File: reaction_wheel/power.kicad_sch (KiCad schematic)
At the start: 3 parts, among them U7 TPS62902RPJR, U9 TPS61379QWRTERQ1

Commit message: things were not working on desktop
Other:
- moved on the sheet: C1, U7
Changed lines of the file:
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@@
 	(paper "A4")
 	(no_connect
-		(at 248.92 39.37)
+		(at 91.44 30.48)
 	)
 	(wire
 		(pts
-			(xy 248.92 41.91) (xy 264.16 41.91)
+			(xy 91.44 33.02) (xy 106.68 33.02)
 		)
 		(stroke
@@
 	(wire
 		(pts
-			(xy 194.31 48.26) (xy 194.31 46.99)
+			(xy 36.83 39.37) (xy 36.83 38.1)
 		)
 		(stroke
@@
 	(wire
 		(pts
-			(xy 264.16 52.07) (xy 264.16 49.53)
+			(xy 106.68 43.18) (xy 106.68 40.64)
 		)
 		(stroke
@@
 	(wire
 		(pts
-			(xy 194.31 46.99) (xy 198.12 46.99)
+			(xy 36.83 38.1) (xy 40.64 38.1)
 		)
 		(stroke
@@
 	(symbol
 		(lib_id "Device:C")
-		(at 264.16 45.72 0)
+		(at 106.68 36.83 0)
 		(unit 1)
 		(body_style 1)
@@
 		(fields_autoplaced yes)
 		(property "Reference" "C1"
-			(at 267.97 44.4499 0)
+			(at 110.49 35.5599 0)
 			(show_name no)
 			(do_not_autoplace no)
@@
 		)
 		(property "Value" "2.2nF"
-			(at 267.97 46.9899 0)
+			(at 110.49 38.0999 0)
 			(show_name no)
 			(do_not_autoplace no)
@@
 		)
 		(property "Footprint" ""
-			(at 265.1252 49.53 0)
+			(at 107.6452 40.64 0)
 			(hide yes)
 			(show_name no)
@@
 		)
 		(property "Datasheet" ""
-			(at 264.16 45.72 0)
+			(at 106.68 36.83 0)
 			(hide yes)
 			(show_name no)
@@
 		)
 		(property "Description" "Unpolarized capacitor"
-			(at 264.16 45.72 0)
+			(at 106.68 36.83 0)
 			(hide yes)
 			(show_name no)
@@
 	(symbol
 		(lib_id "tps62902:TPS62902RPJR")
-		(at 198.12 39.37 0)
+		(at 40.64 30.48 0)
 		(unit 1)
 		(body_style 1)
@@
 		(fields_autoplaced yes)
 		(property "Reference" "U7"
-			(at 223.52 29.21 0)
+			(at 66.04 20.32 0)
 			(show_name no)
 			(do_not_autoplace no)
@@
 		)
 		(property "Value" "TPS62902RPJR"
-			(at 223.52 31.75 0)
+			(at 66.04 22.86 0)
 			(show_name no)
 			(do_not_autoplace no)
@@
 		)
 		(property "Footprint" "QFN_902RPJR_TEX"
-			(at 198.12 39.37 0)
+			(at 40.64 30.48 0)
 			(hide yes)
 			(show_name no)
@@
 		)
 		(property "Datasheet" "https://www.ti.com/lit/gpn/tps62902"
-			(at 198.12 39.37 0)
+			(at 40.64 30.48 0)
 			(hide yes)
 			(show_name no)
@@
 		)
 		(property "Description" ""
-			(at 198.12 39.37 0)
+			(at 40.64 30.48 0)
 			(hide yes)
 			(show_name no)
@@
 	(symbol
 		(lib_id "power:GND")
-		(at 194.31 48.26 0)
+		(at 36.83 39.37 0)
 		(unit 1)
 		(body_style 1)
@@
 		(fields_autoplaced yes)
 		(property "Reference" "#PWR022"
-			(at 194.31 54.61 0)
+			(at 36.83 45.72 0)
 			(hide yes)
 			(show_name no)
@@
 		)
 		(property "Value" "GND"
-			(at 194.31 53.34 0)
+			(at 36.83 44.45 0)
 			(show_name no)
 			(do_not_autoplace no)
@@
 		)
 		(property "Footprint" ""
-			(at 194.31 48.26 0)
+			(at 36.83 39.37 0)
 			(hide yes)
 			(show_name no)
@@
 		)
 		(property "Datasheet" ""
-			(at 194.31 48.26 0)
+			(at 36.83 39.37 0)
 			(hide yes)
 			(show_name no)
@@
 		)
 		(property "Description" "Power symbol creates a global label with name \"GND\" , ground"
-			(at 194.31 48.26 0)
+			(at 36.83 39.37 0)
 			(hide yes)
 			(show_name no)
@@
 	(symbol
 		(lib_id "power:GND")
-		(at 264.16 52.07 0)
+		(at 106.68 43.18 0)
 		(unit 1)
 		(body_style 1)
@@
 		(fields_autoplaced yes)
 		(property "Reference" "#PWR023"
-			(at 264.16 58.42 0)
+			(at 106.68 49.53 0)
 			(hide yes)
 			(show_name no)
@@
 		)
 		(property "Value" "GND"
-			(at 264.16 57.15 0)
+			(at 106.68 48.26 0)
 			(show_name no)
 			(do_not_autoplace no)
@@
 		)
 		(property "Footprint" ""
-			(at 264.16 52.07 0)
+			(at 106.68 43.18 0)
 			(hide yes)
 			(show_name no)
@@
 		)
 		(property "Datasheet" ""
-			(at 264.16 52.07 0)
+			(at 106.68 43.18 0)
 			(hide yes)
 			(show_name no)
@@
 		)
 		(property "Description" "Power symbol creates a global label with name \"GND\" , ground"
-			(at 264.16 52.07 0)
-			(hide yes)
-			(show_name no)
+			(at 106.68 43.18 0)
+			(hide yes)
+			(show_name no)

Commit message: Add files via upload
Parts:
- removed C1: 2.2nF, symbol Device:C
- removed U7: TPS62902RPJR, QFN_902RPJR_TEX, symbol tps62902:TPS62902RPJR
- removed U9: TPS61379QWRTERQ1, RTE0016K-IPC_A, symbol TPS62902RPJR_boost_converter:TPS61379QWRTERQ1
- added C36: 10uF, symbol Device:C
- added C37: 10nF, symbol Device:C
- added C38, C39, C44: 22uF, symbol Device:C
- added C40: 4.7nF, symbol Device:C
- added C41: 0.1uF, symbol Device:C
- added C42: 2.2uF, symbol Device:C
- added C43: 1uF, symbol Device:C
- added J12: 5013310207, CONN_5013310000-SD_02_MOL, symbol molex_pico_clasp:5013310207
- added L5, L6: 1uH, symbol Device:L
- added R27: 26.1k, symbol Device:R
- added R35, R37: 100k, symbol Device:R
- added R36: 10k, symbol Device:R
- added R38: 18k, symbol Device:R
- added R39: 280k, symbol Device:R
- added R40: 20k, symbol Device:R
- added U12: TPS62902RPJR, QFN_902RPJR_TEX, symbol tps62902:TPS62902RPJR
- added U13: TPS61379QWRTERQ1, RTE0016K-IPC_A, symbol TPS62902RPJR_boost_converter:TPS61379QWRTERQ1
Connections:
- net GND: now also C36.2, C37.2, C38.2, C39.2, C40.2, C42.2, C43.2, C44.2, J12.2, R27.2, R38.2, R40.2, U12.4 (GND), U13.17 (Thermal_Pad), U13.5 (MODE_SYNC), U13.7 (GND), U13.8 (GND)
- new net: C40.1, R36.2
- new net +12V: C43.1, C44.1, R39.1, U13.10 (OUT), U13.9 (VO)
- new net +3V3: C38.1, L5.2, U12.3 (VOS)
- new net BST_Boost: C41.2, U13.2 (BST)
- new net COMP_Boost: R36.1, U13.14 (COMP)
- new net EN_Boost: R35.2, U13.15 (EN)
- new net FB_Boost: R39.2, R40.1, U13.13 (FB)
- new net FREQ_Boost: R38.1, U13.16 (FREQ)
- new net MODE_SCONF_Buck: R27.1, U12.7 (MODE/S-CONF)
- new net PG_Boost: R37.1, U13.11 (PG)
- new net SS_TR_Buck: C37.1, U12.8 (SS/TR)
- new net SW_Boost: C41.1, L6.2, U13.3 (SW), U13.4 (SW)
- new net SW_Buck: L5.1, U12.2 (SW)
- new net VBATT: C36.1, C39.1, J12.1, L6.1, R35.1, U12.5 (EN), U12.6 (VIN), U13.1 (VIN)
- new net VCC_Boost: C42.1, R37.2, U13.6 (VCC)
- no-connect marks 1 -> 3
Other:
- note added: "Battery Connector to ADCS Board"
- note added: "Boost Converter: Battery to +12V"
- note added: "Buck Converter: Battery to +3V3"
- note added: "For C27 (10uF cap), select a ceramic capacitor rated for at least 16V or 25V (X7R or X5R dielectric). Ceramic capacitors lose effective capacitance under DC bias voltage; a 10V-rated capacitor will drop below the minimum required capacitance when operating at 8V input."
- note added: "SS/TR: do i need soft time start thing? for 1ms = 10nF else can leave open?"
- note added: "molex pico clasp connector"

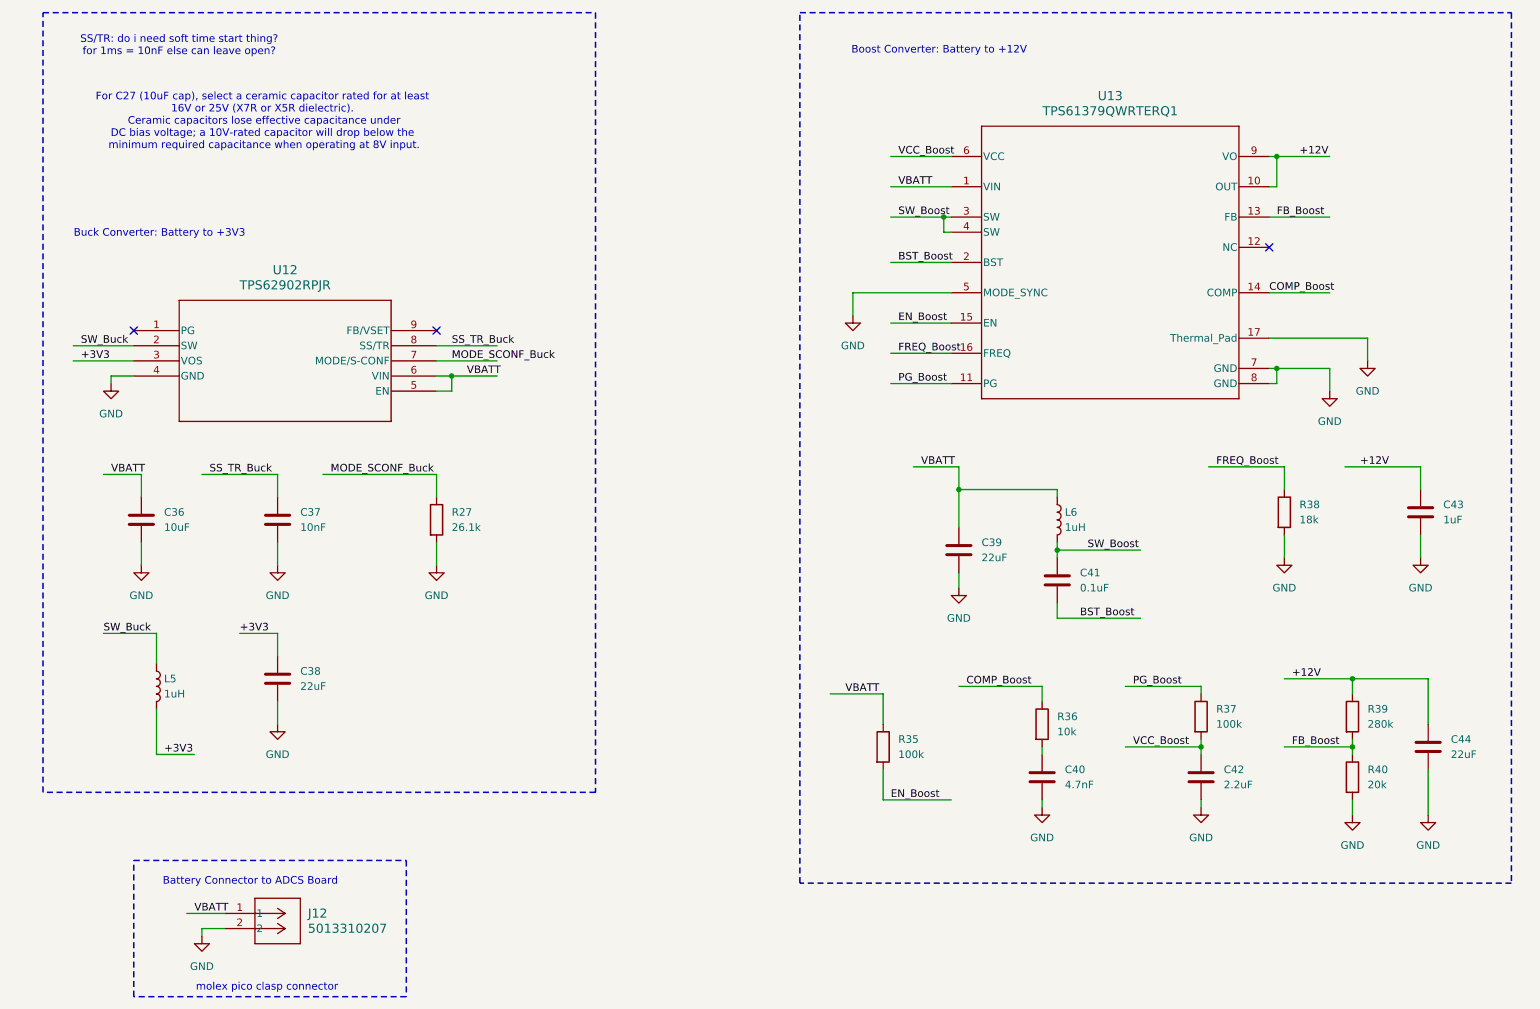
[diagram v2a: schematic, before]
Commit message: clean up sch, notes, added parts minus stlink
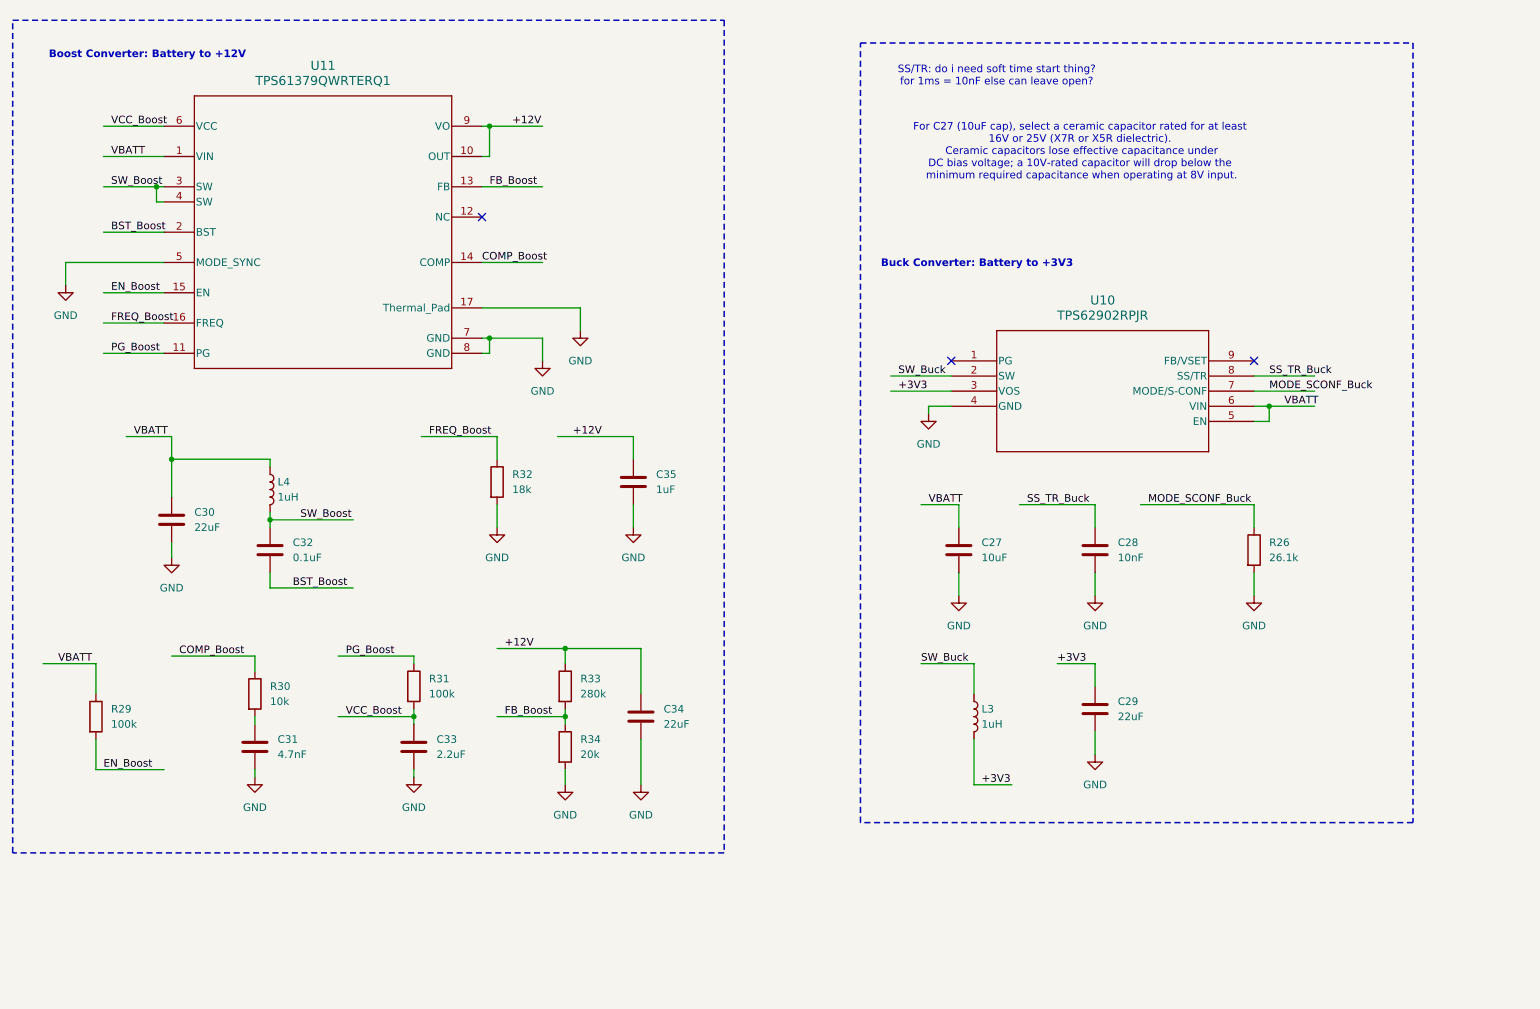
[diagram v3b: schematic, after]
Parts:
- removed C36: 10uF, symbol Device:C
- removed C37: 10nF, symbol Device:C
- removed C38, C39, C44: 22uF, symbol Device:C
- removed C40: 4.7nF, symbol Device:C
- removed C41: 0.1uF, symbol Device:C
- removed C42: 2.2uF, symbol Device:C
- removed C43: 1uF, symbol Device:C
- removed J12: 5013310207, CONN_5013310000-SD_02_MOL, symbol molex_pico_clasp:5013310207
- removed L5, L6: 1uH, symbol Device:L
- removed R27: 26.1k, symbol Device:R
- removed R35, R37: 100k, symbol Device:R
- removed R36: 10k, symbol Device:R
- removed R38: 18k, symbol Device:R
- removed R39: 280k, symbol Device:R
- removed R40: 20k, symbol Device:R
- removed U12: TPS62902RPJR, QFN_902RPJR_TEX, symbol tps62902:TPS62902RPJR
- removed U13: TPS61379QWRTERQ1, RTE0016K-IPC_A, symbol TPS62902RPJR_boost_converter:TPS61379QWRTERQ1
- added C27: 10uF, symbol Device:C
- added C28: 10nF, symbol Device:C
- added C29, C30, C34: 22uF, symbol Device:C
- added C31: 4.7nF, symbol Device:C
- added C32: 0.1uF, symbol Device:C
- added C33: 2.2uF, symbol Device:C
- added C35: 1uF, symbol Device:C
- added L3, L4: 1uH, symbol Device:L
- added R26: 26.1k, symbol Device:R
- added R29, R31: 100k, symbol Device:R
- added R30: 10k, symbol Device:R
- added R32: 18k, symbol Device:R
- added R33: 280k, symbol Device:R
- added R34: 20k, symbol Device:R
- added U10: TPS62902RPJR, QFN_902RPJR_TEX, symbol tps62902:TPS62902RPJR
- added U11: TPS61379QWRTERQ1, RTE0016K-IPC_A, symbol TPS62902RPJR_boost_converter:TPS61379QWRTERQ1
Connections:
- net +12V: now also C34.1, C35.1, R33.1, U11.10 (OUT), U11.9 (VO)
- net +3V3: now also C29.1, L3.2, U10.3 (VOS)
- net BST_Boost: now also C32.2, U11.2 (BST)
- net COMP_Boost: now also R30.1, U11.14 (COMP)
- net EN_Boost: now also R29.2, U11.15 (EN)
- net FB_Boost: now also R33.2, R34.1, U11.13 (FB)
- net FREQ_Boost: now also R32.1, U11.16 (FREQ)
- net GND: now also C27.2, C28.2, C29.2, C30.2, C31.2, C33.2, C34.2, C35.2, R26.2, R32.2, R34.2, U10.4 (GND), U11.17 (Thermal_Pad), U11.5 (MODE_SYNC), U11.7 (GND), U11.8 (GND)
- net MODE_SCONF_Buck: now also R26.1, U10.7 (MODE/S-CONF)
- net PG_Boost: now also R31.1, U11.11 (PG)
- net SS_TR_Buck: now also C28.1, U10.8 (SS/TR)
- net SW_Boost: now also C32.1, L4.2, U11.3 (SW), U11.4 (SW)
- net SW_Buck: now also L3.1, U10.2 (SW)
- net VBATT: now also C27.1, C30.1, L4.1, R29.1, U10.5 (EN), U10.6 (VIN), U11.1 (VIN)
- net VCC_Boost: now also C33.1, R31.2, U11.6 (VCC)
- new net: C31.1, R30.2
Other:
- note removed: "Battery Connector to ADCS Board"
- note removed: "molex pico clasp connector"

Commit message: added notes
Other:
- note added: "For C27 (10uF cap), select a ceramic capacitor rated for at least 16V or 25V (X7R or X5R dielectric). Ceramic capacitors lose effective capacitance under DC bias voltage; a 10V-rated capacitor will drop below the minimum required capacitance when operating at 8V input. ---> not sure if this is important? or needed?"
- note removed: "For C27 (10uF cap), select a ceramic capacitor rated for at least 16V or 25V (X7R or X5R dielectric). Ceramic capacitors lose effective capacitance under DC bias voltage; a 10V-rated capacitor will drop below the minimum required capacitance when operating at 8V input."
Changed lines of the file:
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@@
 		)
 	)
-	(text "For C27 (10uF cap), select a ceramic capacitor rated for at least \n16V or 25V (X7R or X5R dielectric).\n Ceramic capacitors lose effective capacitance under \nDC bias voltage; a 10V-rated capacitor will drop below the\n minimum required capacitance when operating at 8V input."
+	(text "For C27 (10uF cap), select a ceramic capacitor rated for at least \n16V or 25V (X7R or X5R dielectric).\n Ceramic capacitors lose effective capacitance under \nDC bias voltage; a 10V-rated capacitor will drop below the\n minimum required capacitance when operating at 8V input.\n---> not sure if this is important? or needed? "
 		(exclude_from_sim no)
 		(at 199.39 38.608 0)

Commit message: got to layout
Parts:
- C1: renamed from C30; footprint (none) -> Capacitor_SMD:C_0603_1608Metric
- C2: renamed from C31; footprint (none) -> Capacitor_SMD:C_0603_1608Metric
- C3: renamed from C32; footprint (none) -> Capacitor_SMD:C_0603_1608Metric
- C4: renamed from C33; footprint (none) -> Capacitor_SMD:C_0603_1608Metric
- C5: renamed from C35; footprint (none) -> Capacitor_SMD:C_0603_1608Metric
- C6: renamed from C34; footprint (none) -> Capacitor_SMD:C_0603_1608Metric
- C7: renamed from C27; footprint (none) -> Capacitor_SMD:C_0603_1608Metric
- C8: renamed from C28; footprint (none) -> Capacitor_SMD:C_0603_1608Metric
- C9: renamed from C29; footprint (none) -> Capacitor_SMD:C_0603_1608Metric
- L1: renamed from L4; footprint (none) -> Inductor_SMD:L_0603_1608Metric
- L2: renamed from L3; footprint (none) -> Inductor_SMD:L_0603_1608Metric
- R1: renamed from R29; footprint (none) -> Resistor_SMD:R_0603_1608Metric
- R2: renamed from R30; footprint (none) -> Resistor_SMD:R_0603_1608Metric
- R3: renamed from R31; footprint (none) -> Resistor_SMD:R_0603_1608Metric
- R4: renamed from R32; footprint (none) -> Resistor_SMD:R_0603_1608Metric
- R5: renamed from R33; footprint (none) -> Resistor_SMD:R_0603_1608Metric
- R6: renamed from R34; footprint (none) -> Resistor_SMD:R_0603_1608Metric
- R7: renamed from R26; footprint (none) -> Resistor_SMD:R_0603_1608Metric
- U1: renamed from U11; footprint RTE0016K-IPC_A -> sidrishaLibrary:RTE0016K-IPC_B
- U2: renamed from U10; footprint QFN_902RPJR_TEX -> sidrishaLibrary:QFN_902RPJR_TEX
